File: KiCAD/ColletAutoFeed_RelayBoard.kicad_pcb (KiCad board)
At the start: 2 copper layers, 117.2 x 159.5 mm, 55 parts, among them J1 XW4M-10D2-H1DS, J2 XW4M-02D1-H1DA, K1 G5V-1, K2 G5V-1, K3 G5V-1, K4 G5V-1, K5 G5V-1, K6 G5V-1, K7 G5V-1, K8 G5V-1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

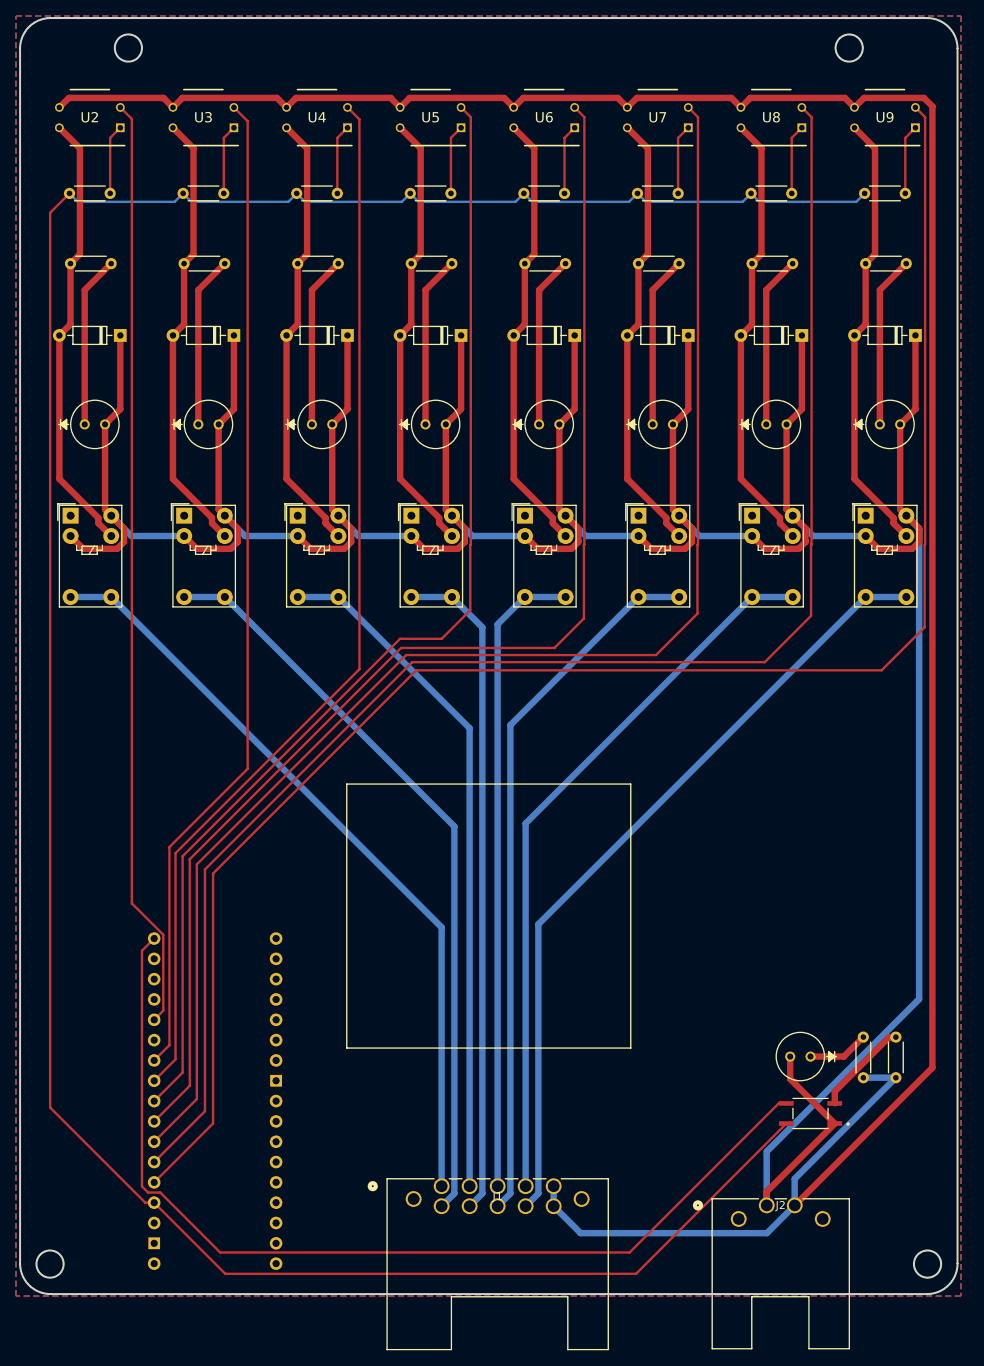
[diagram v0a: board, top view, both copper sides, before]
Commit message: Replaced remaining opto-isolator and started silkscreen
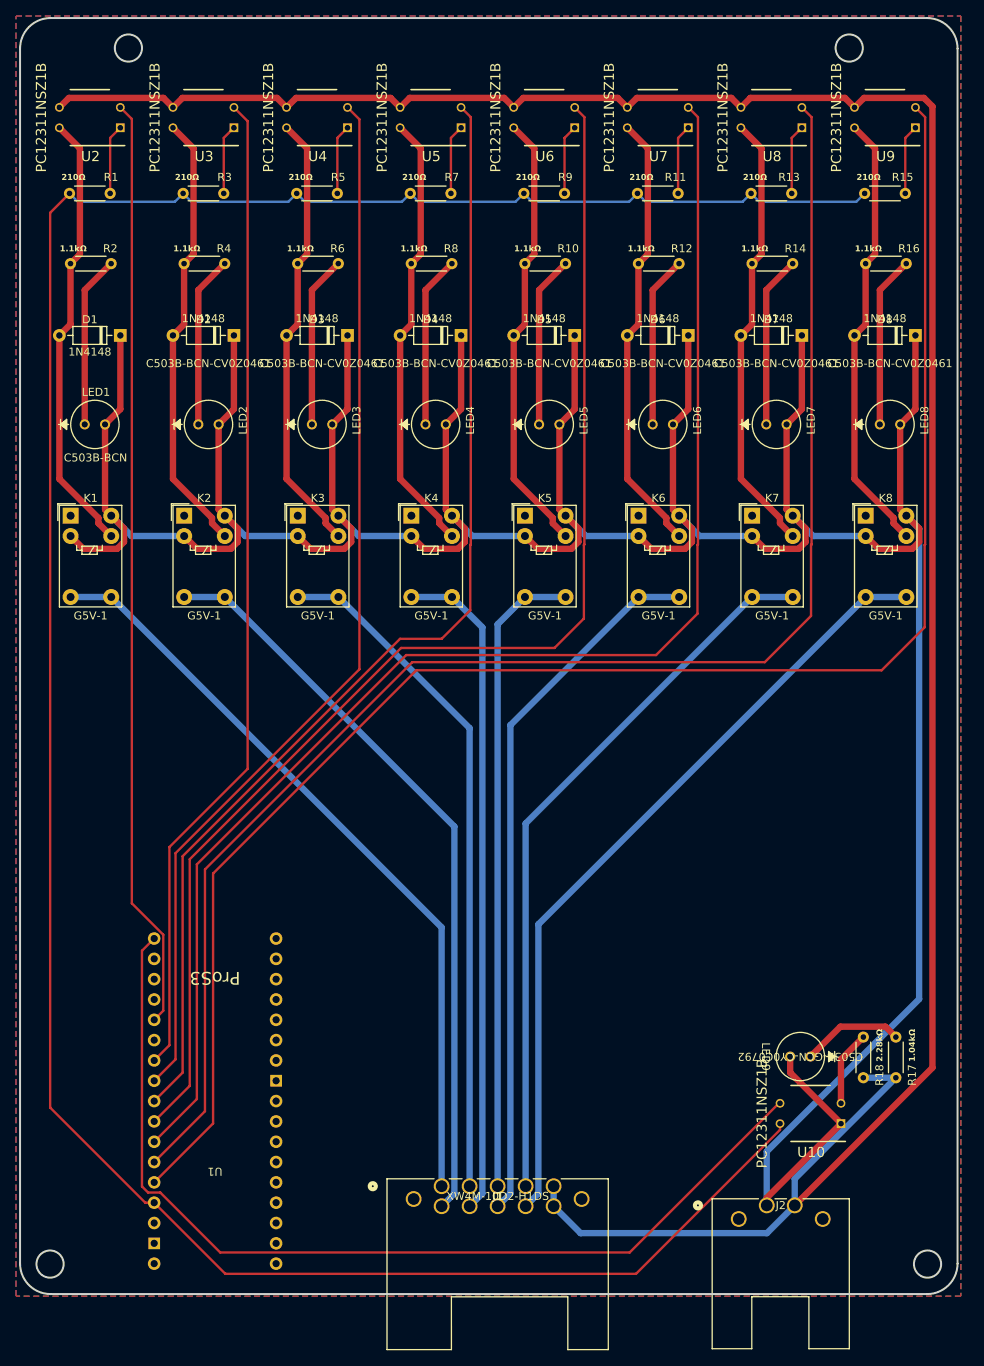
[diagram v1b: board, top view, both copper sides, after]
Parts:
- LED1: value C503B-BCN-CV0Z0461 -> C503B-BCN
- R17: value 2.28kΩ -> 1.04kΩ
- R18: value 1.04kΩ -> 2.28kΩ
- U10: value PC365NJ0000F -> PC12311NSZ1B; footprint PC365NJ0000F:PC365NJ0000F -> PC12311NSZ1B:PC12311NSZ1B
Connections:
- R17 pad 1: Net-(R17-Pad1) -> Net-(LED9-Pad1)
- R18 pad 1: Net-(LED9-Pad1) -> Net-(R18-Pad1)
- U10 pad 2: Net-(R17-Pad1) -> Net-(R18-Pad1)
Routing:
- net Net-(R17-Pad1): track 11.9 -> 0.00 mm
- net Net-(R18-Pad1): track 0.00 -> 9.44 mm
- net Net-(LED9-Pad1): track 7.61 -> 12.8 mm
- net /IO12: track 123.3 -> 122.4 mm
- net +24V: track 472.7 -> 473.3 mm

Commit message: Fixed Silkscreen Labels for Components
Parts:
- D1, D2, D3, D4, D5, D6, D7, D8: footprint Diode_THT:D_DO-35_SOD27_P7.62mm_Horizontal -> Diode_THT:D_DO-35_SOD27_P7.62mm_Horizontal-JW
- LED2, LED3, LED4, LED5, LED6, LED7, LED8: value C503B-BCN-CV0Z0461 -> C503B-BCN
- LED9: value C503B-GCN-CY0C0792 -> C503B-GCN
- moved LED9 8.20 mm to (129.3, 145.9)
- moved U10 5.53 mm to (128.8, 157.4)
- moved R18 2.44 mm to (139.1, 148.3)
- moved R17 2.41 mm to (145.0, 148.2)
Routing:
- net GND: track 322.2 -> 311.2 mm
- net +24V: track 473.3 -> 478.2 mm
- net /MCU 3.3v: track 328.8 -> 324.7 mm
- net Net-(LED9-Pad1): track 12.8 -> 16.6 mm
- net /IO12: track 122.4 -> 118.8 mm
- net Net-(R18-Pad1): track 9.44 -> 10.9 mm

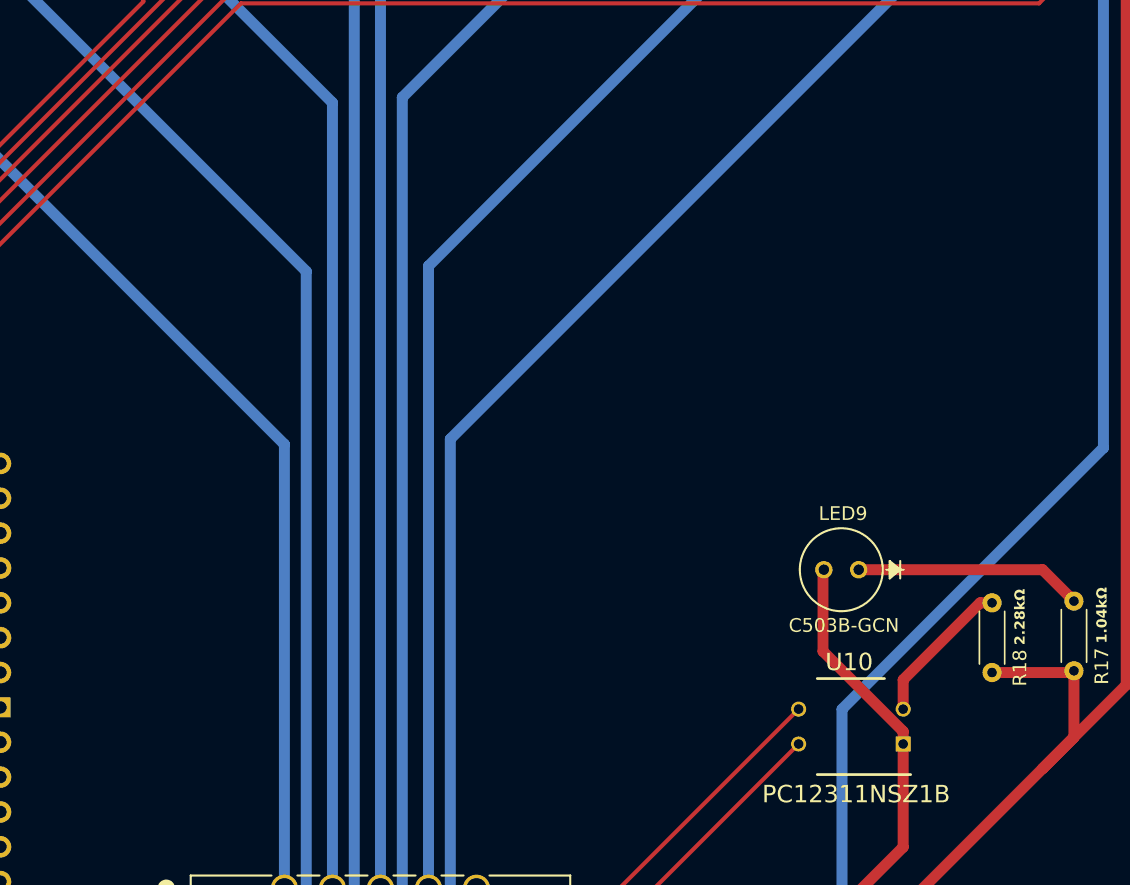
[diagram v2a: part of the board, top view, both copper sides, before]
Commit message: Update ColletAutoFeed_RelayBoard.kicad_pcb
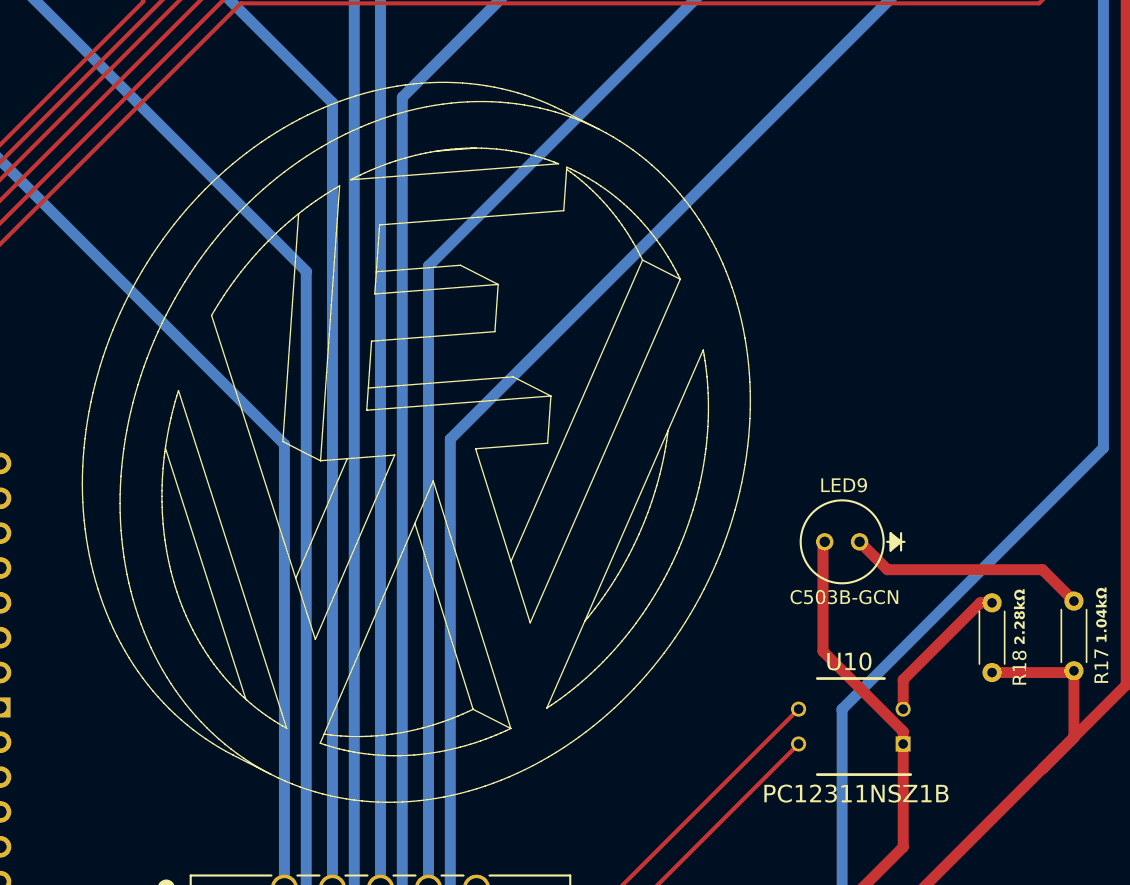
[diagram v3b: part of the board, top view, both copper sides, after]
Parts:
- moved LED9 2.03 mm to (129.4, 143.9)
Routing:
- net +24V: track 478.2 -> 480.2 mm
- net Net-(LED9-Pad1): track 16.6 -> 17.4 mm

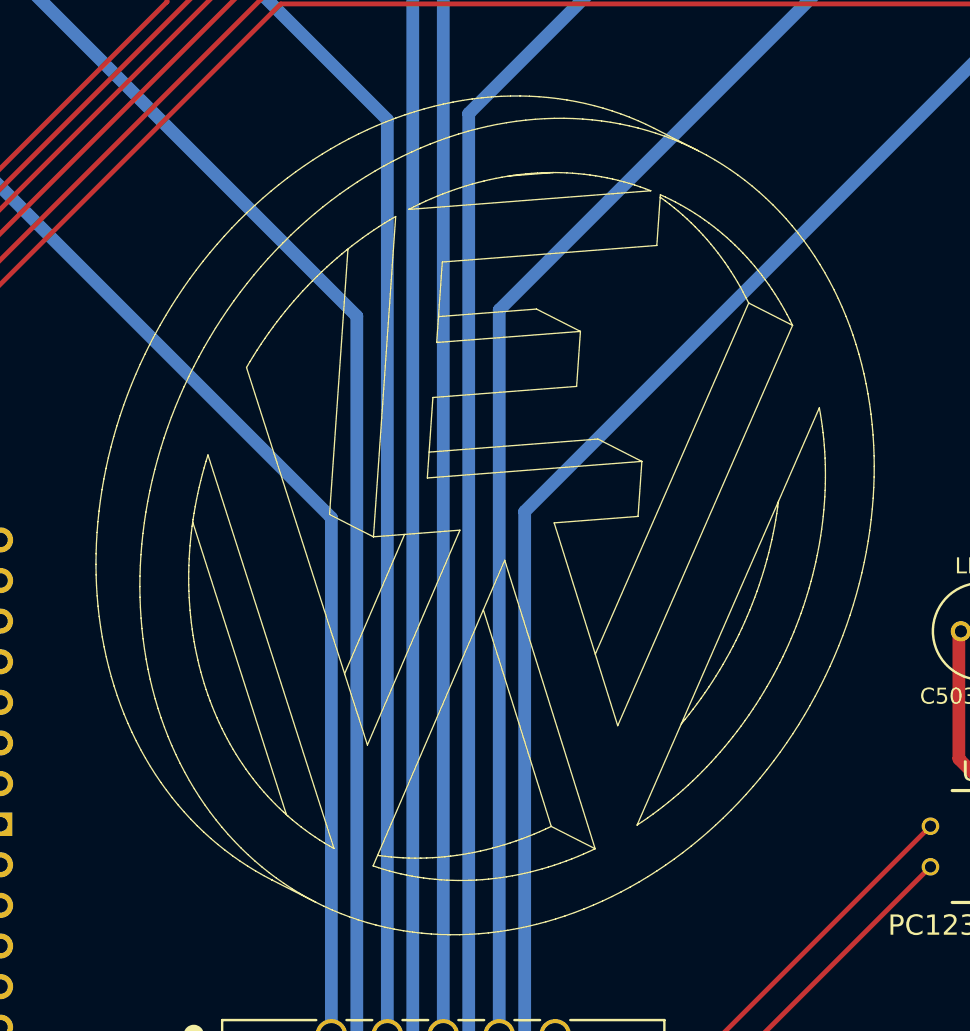
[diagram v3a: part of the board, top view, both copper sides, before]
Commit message: Added Logo to silkscreen
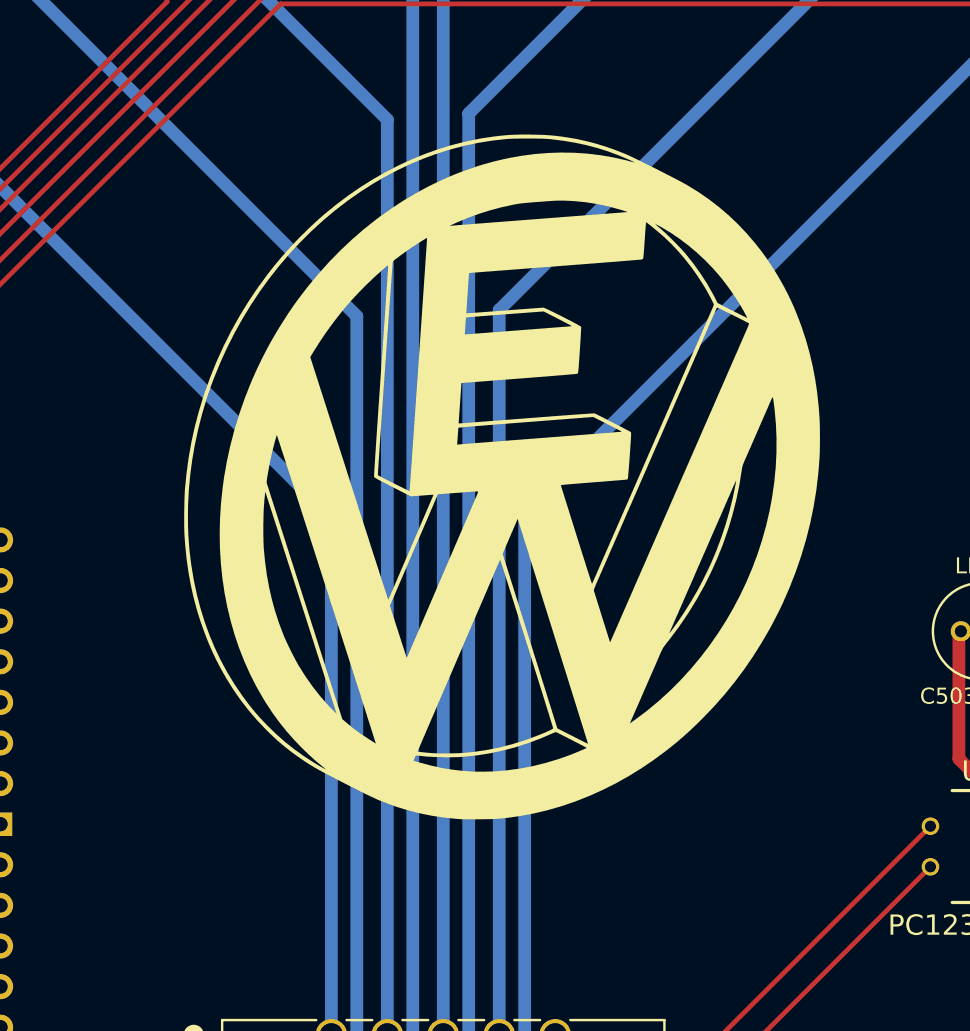
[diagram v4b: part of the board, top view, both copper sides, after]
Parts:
- added G***: LOGO, Warner Consulting Logo:Warner Consulting Logo, F.Cu at (98.2, 134.2)

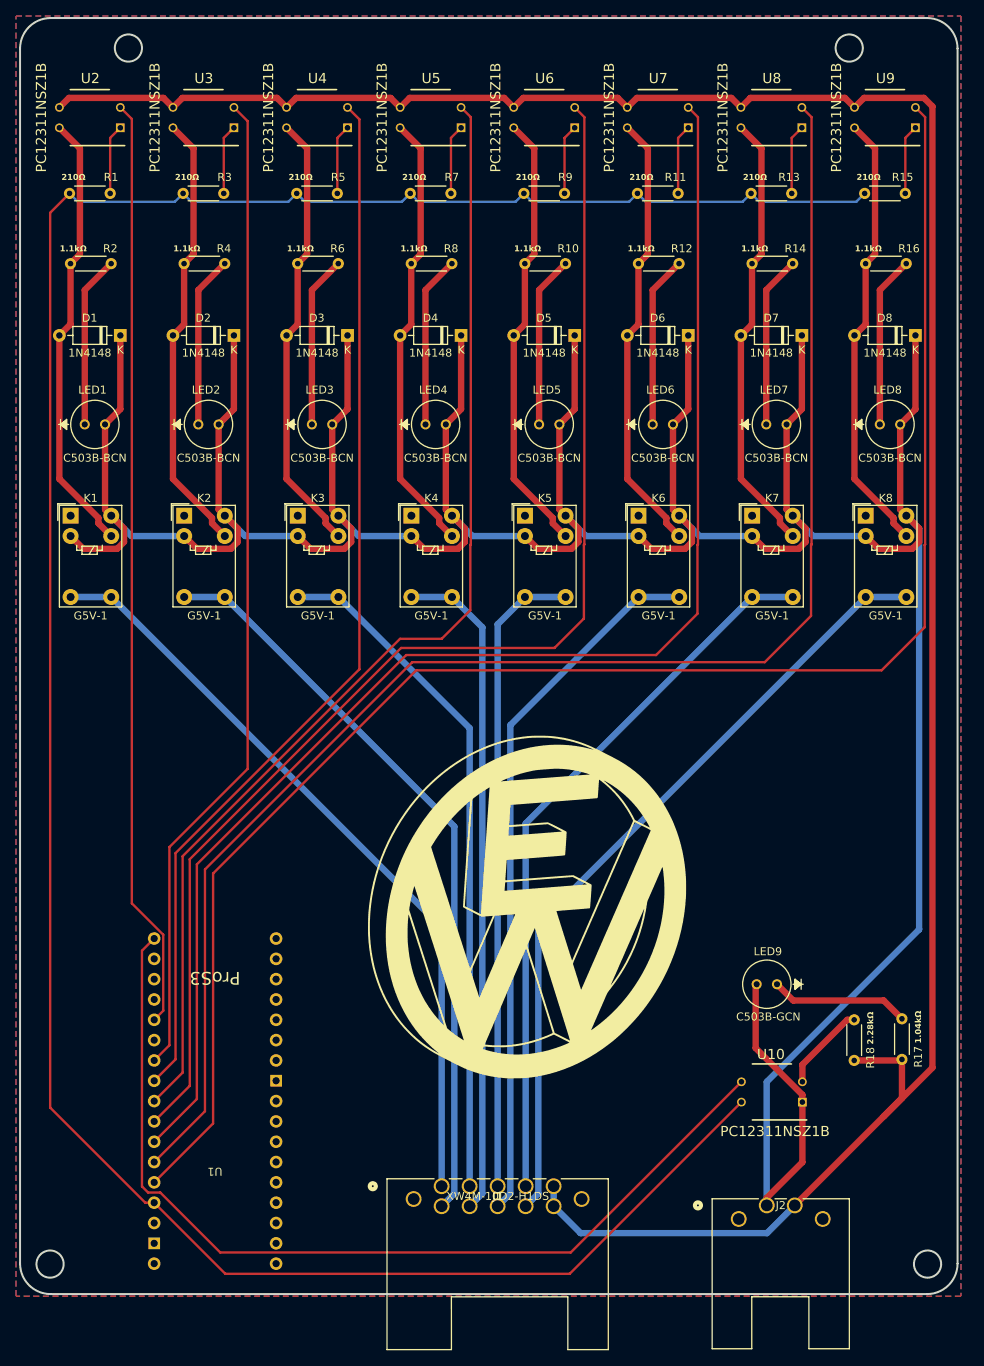
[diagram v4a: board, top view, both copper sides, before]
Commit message: Added zones and labels to Silkscreen
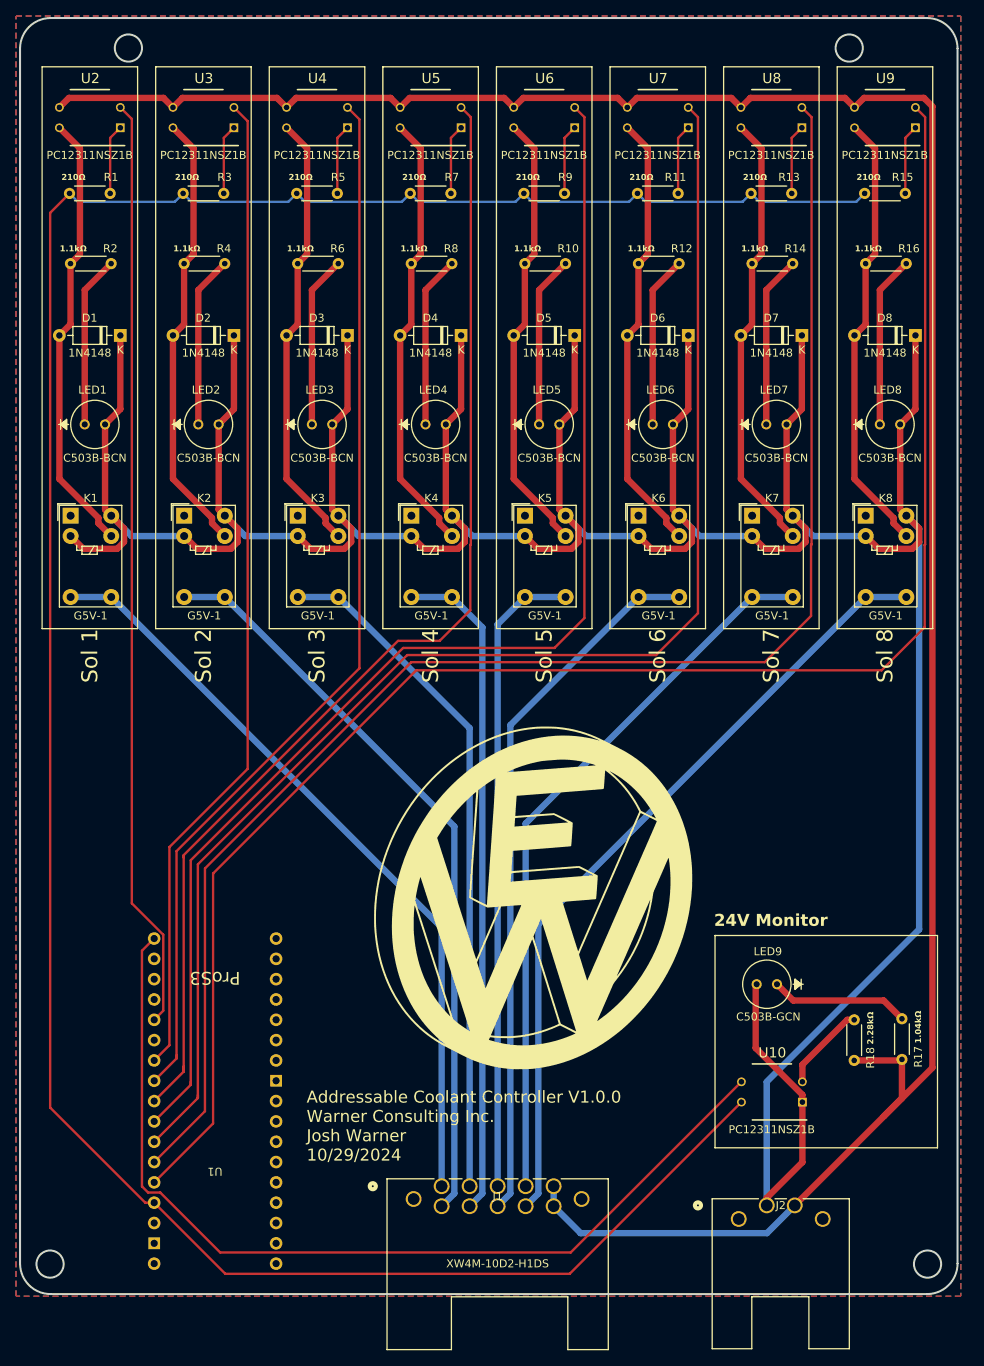
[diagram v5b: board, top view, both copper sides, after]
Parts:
- moved G*** 1.37 mm to (98.9, 133.1)
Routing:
- net /IO5: track 144.2 -> 144.9 mm
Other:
- board text added: "24V Monitor"
- board text added: "Addressable Coolant Controller V1.0.0 Warner Consulting Inc. Josh Warner 10/29/2024"
- board text added: "Sol 1"
- board text added: "Sol 2"
- board text added: "Sol 3"
- board text added: "Sol 4"
- board text added: "Sol 5"
- board text added: "Sol 6"
- board text added: "Sol 7"
- board text added: "Sol 8"
